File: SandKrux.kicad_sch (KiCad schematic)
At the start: 108 parts, among them CN2 SM02B-PASS-TBT(LF)(SN), CN3 1.25mm-2P socket, IC1 TROPIC01_chip, Q1 S8050, SW1 TL3330AF130QG, SW2 TL3330AF130QG, SW3 TL3330AF130QG, SW4 TL3330AF130QG, SW5 TL3330AF130QG, U10 AXP173_C3345106, U13 CH552T, U2 MT9700, U3 XC6206-3.3V, U9 HX TF-CARD XG8P H1.5

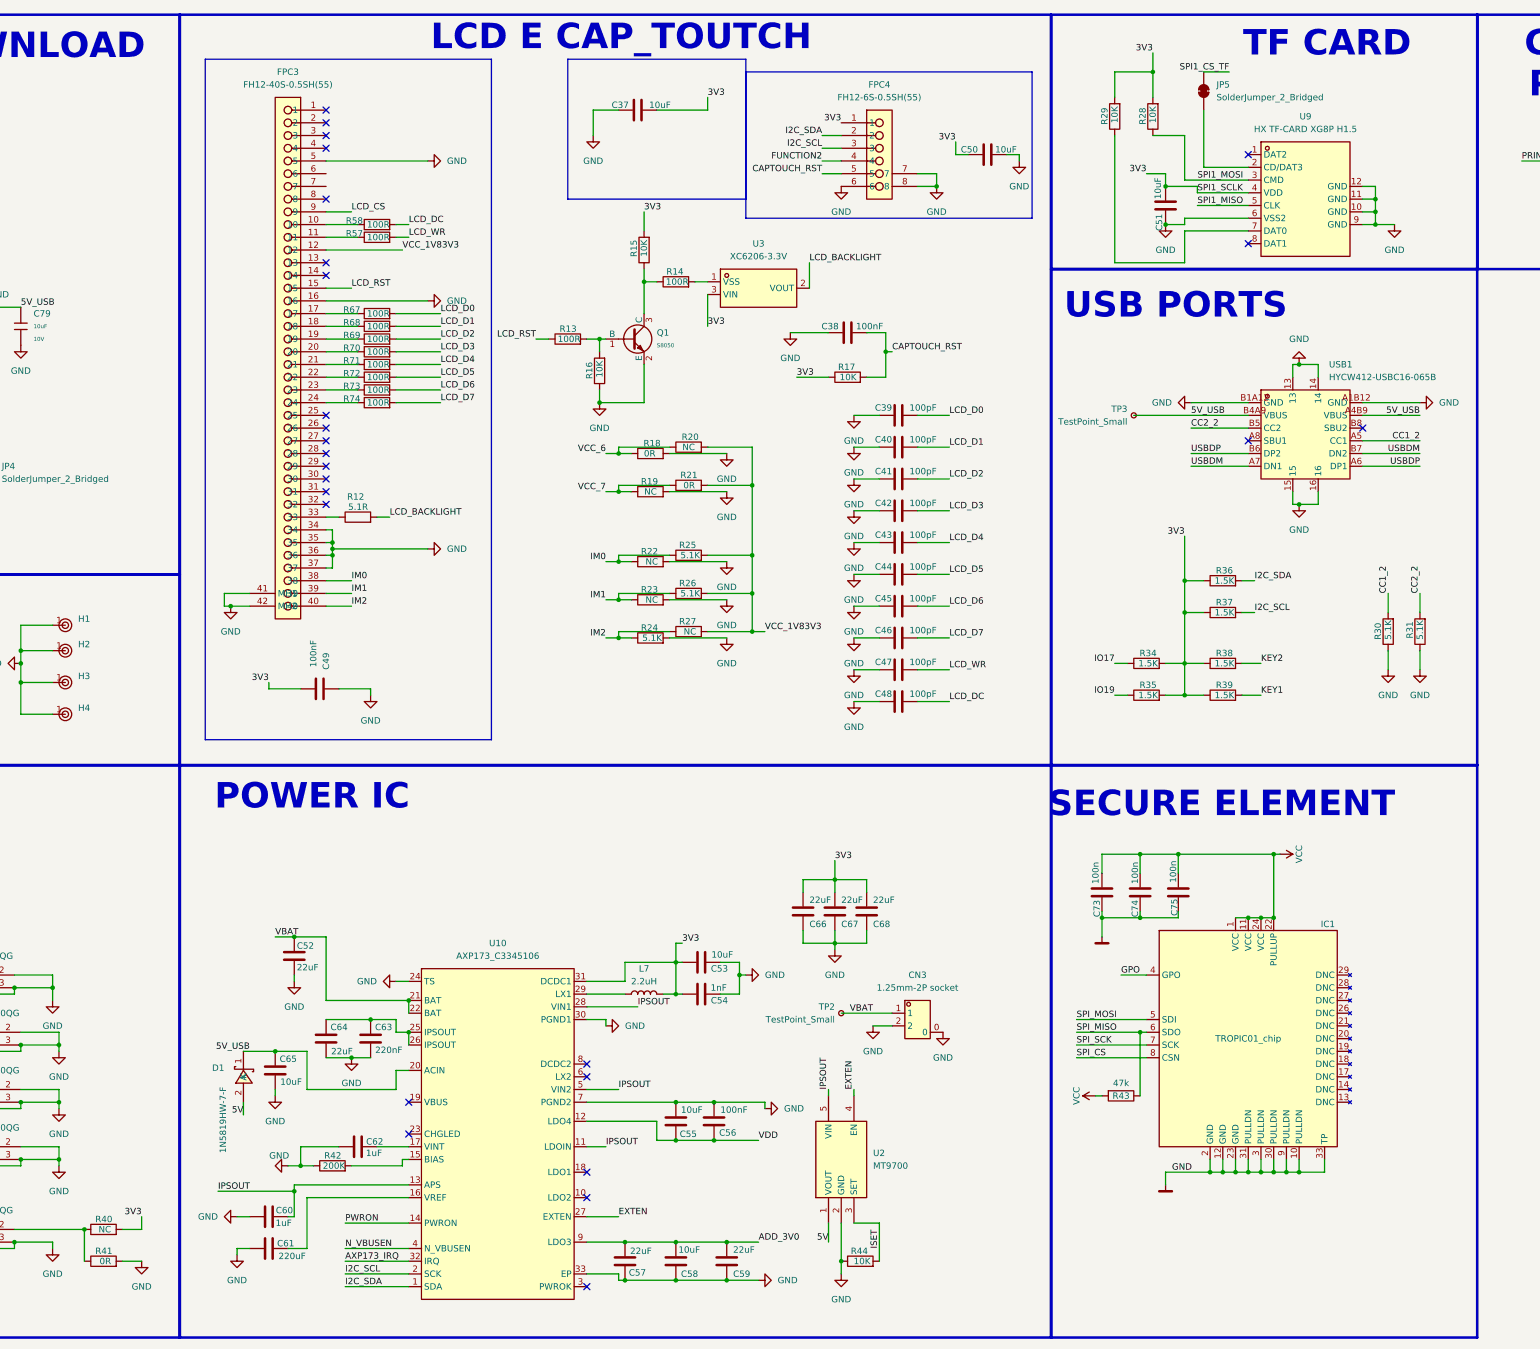
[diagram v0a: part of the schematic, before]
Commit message: troca de resistores por pecas jlcpcb
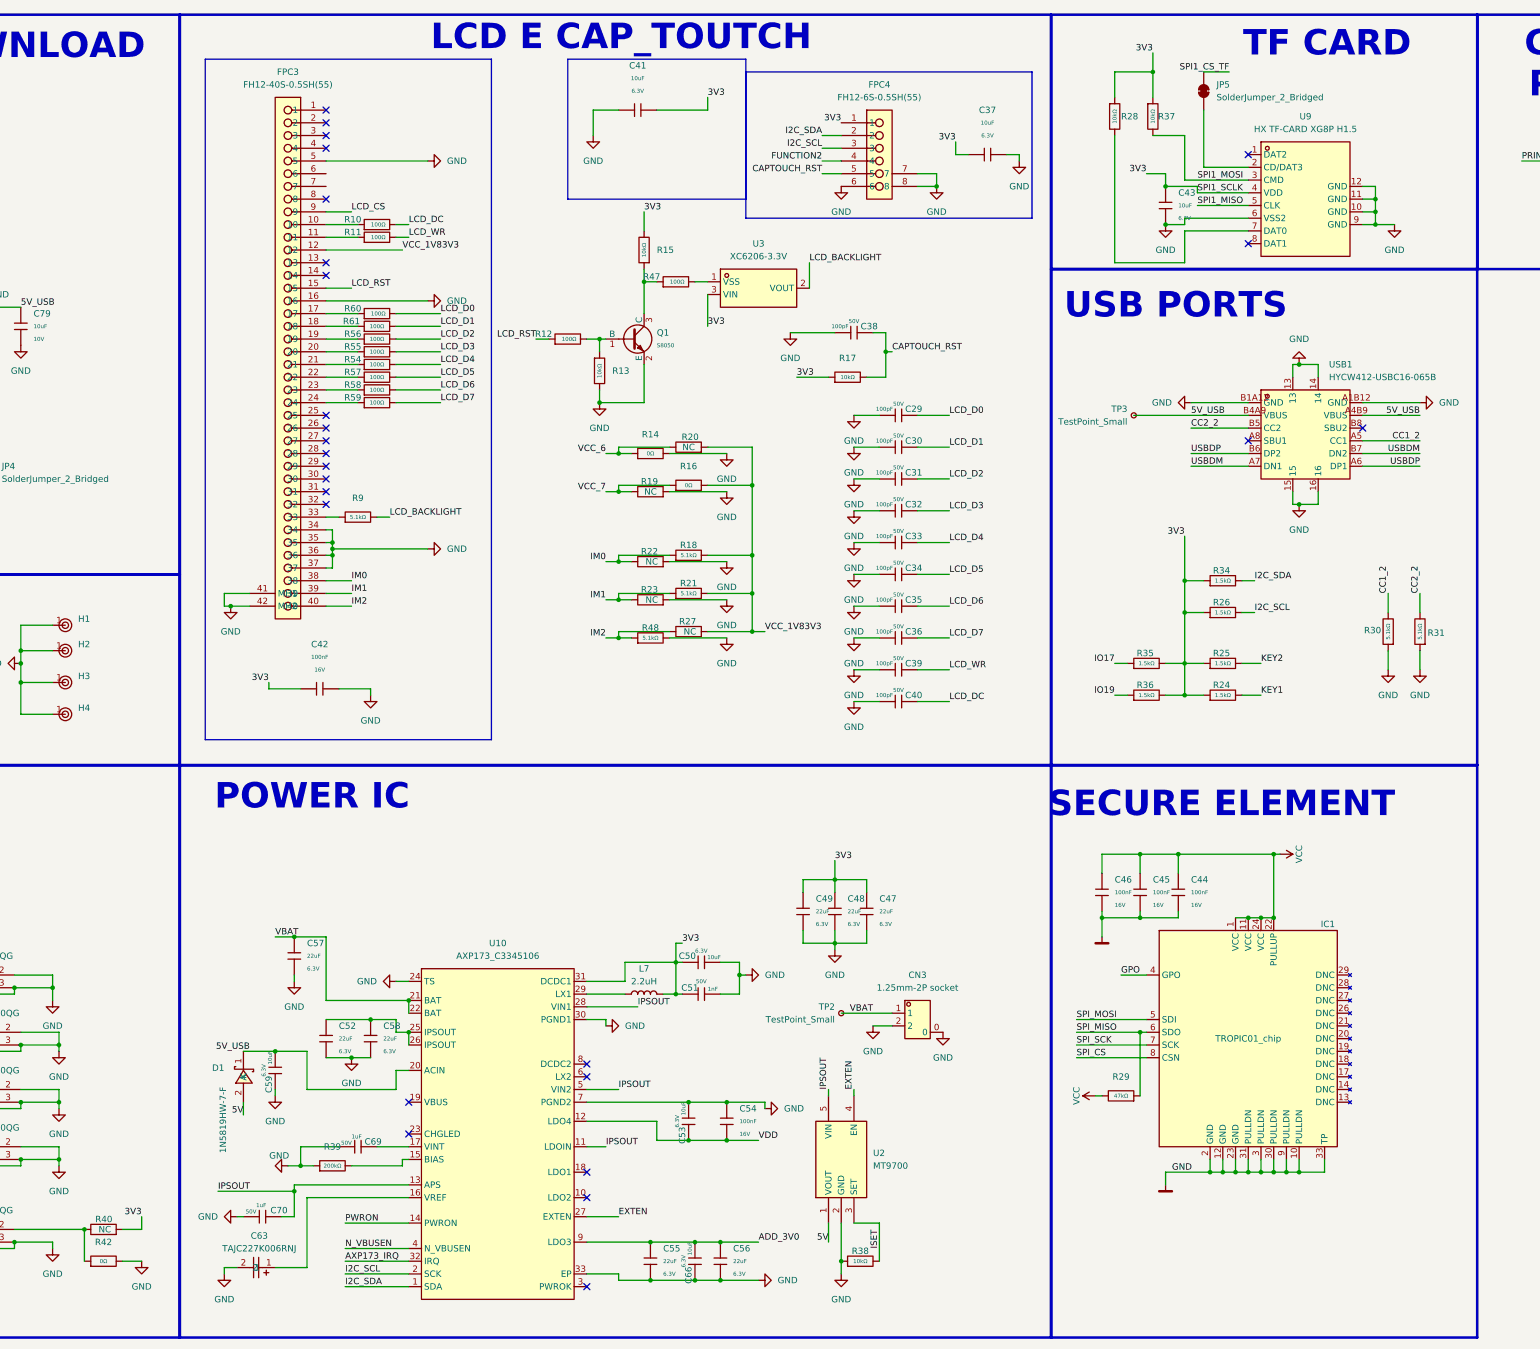
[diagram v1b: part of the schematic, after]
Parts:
- removed C37, C50, C51, C53, C55, C58, C65: 10uF, Capacitor_SMD:C_0201_0603Metric, symbol Device:C
- removed C38, C49, C56: 100nF, Capacitor_SMD:C_0201_0603Metric, symbol Device:C
- removed C39, C40, C41, C42, C43, C44, C45, C46, C47, C48: 100pF, Capacitor_SMD:C_0201_0603Metric, symbol Device:C
- removed C52, C57, C59, C64, C66, C67, C68: 22uF, Capacitor_SMD:C_0201_0603Metric, symbol Device:C
- removed C54: 1nF, Capacitor_SMD:C_0201_0603Metric, symbol Device:C
- removed C60, C62: 1uF, Capacitor_SMD:C_0201_0603Metric, symbol Device:C
- removed C61: 220uF, Capacitor_SMD:C_0201_0603Metric, symbol Device:C
- removed C63: 220nF, Capacitor_SMD:C_0201_0603Metric, symbol Device:C
- removed C73, C74, C75: 100n, Capacitor_SMD:C_0402_1005Metric, symbol Device:C
- removed R12: 5.1R, Resistor_SMD:R_0201_0603Metric, symbol Device:R
- removed R13, R14, R57, R58, R67, R68, R69, R70, R71, R72, R73, R74: 100R, Resistor_SMD:R_0201_0603Metric, symbol Device:R
- removed R15, R16, R17, R28, R29, R44: 10K, Resistor_SMD:R_0201_0603Metric, symbol Device:R
- removed R18, R21, R41: 0R, Resistor_SMD:R_0201_0603Metric, symbol Device:R
- removed R24, R25, R26, R30, R31: 5.1K, Resistor_SMD:R_0201_0603Metric, symbol Device:R
- removed R34, R35, R36, R37, R38, R39: 1.5K, Resistor_SMD:R_0201_0603Metric, symbol Device:R
- removed R42: 200K, Resistor_SMD:R_0201_0603Metric, symbol Device:R
- removed R43: 47k, Resistor_SMD:R_0402_1005Metric, symbol Device:R
- added C29, C30, C31, C32, C33, C34, C35, C36, C38, C39, C40: 100pF, PCM_JLCPCB:C_0402, symbol PCM_JLCPCB-Capacitors:0402,100pF
- added C37, C41, C43, C50, C53, C59, C66: 10uF, PCM_JLCPCB:C_0402, symbol PCM_JLCPCB-Capacitors:0402,10uF
- added C42, C44, C45, C46, C54: 100nF, PCM_JLCPCB:C_0402, symbol PCM_JLCPCB-Capacitors:0402,100nF
- added C47, C48, C49, C52, C55, C56, C57, C58: 22uF, PCM_JLCPCB:C_0603, symbol PCM_JLCPCB-Capacitors:0603,22uF
- added C51: 1nF, PCM_JLCPCB:C_0402, symbol PCM_JLCPCB-Capacitors:0402,1nF
- added C63: TAJC227K006RNJ, easyeda2kicad:CAP-SMD_L6.0-W3.2-R-RD, symbol easyeda2kicad:TAJC227K006RNJ
- added C69, C70: 1uF, PCM_JLCPCB:C_0603, symbol PCM_JLCPCB-Capacitors:0603,1uF
- added R10, R11, R12, R47, R54, R55, R56, R57, R58, R59, R60, R61: 100Ω, PCM_JLCPCB:R_0402, symbol PCM_JLCPCB-Resistors:0402,100Ω
- added R13, R15, R17, R28, R37, R38: 10kΩ, PCM_JLCPCB:R_0402, symbol PCM_JLCPCB-Resistors:0402,10kΩ
- added R14, R16, R42: 0Ω, PCM_JLCPCB:R_0402, symbol PCM_JLCPCB-Resistors:0402,0Ω
- added R18, R21, R30, R31, R48, R9: 5.1kΩ, PCM_JLCPCB:R_0402, symbol PCM_JLCPCB-Resistors:0402,5.1kΩ
- added R24, R25, R26, R34, R35, R36: 1.5kΩ, PCM_JLCPCB:R_0402, symbol PCM_JLCPCB-Resistors:0402,1.5kΩ
- added R29: 47kΩ, PCM_JLCPCB:R_0402, symbol PCM_JLCPCB-Resistors:0402,47kΩ
- added R39: 200kΩ, PCM_JLCPCB:R_0402, symbol PCM_JLCPCB-Resistors:0402,200kΩ
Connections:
- net 3V3: now also C37.1, C41.2, C42.1, C43.1, C47.1, C48.1, C49.1, C50.1, C51.1, R15.2, R17.1, R24.1, R25.1, R26.1, R28.1, R34.1, R35.2, R36.2, R37.1
- net 5V_USB: now also C59.2
- net ADD_3V0: now also C55.1, C56.1, C66.2
- net CAPTOUCH_RST: now also C38.2, R17.2
- net CC1_2: now also R30.2
- net CC2_2: now also R31.2
- net GND: now also C29.1, C30.1, C31.1, C32.1, C33.1, C34.1, C35.1, C36.1, C37.2, C38.1, C39.1, C40.1, C41.1, C42.2, C43.2, C44.2, C45.2, C46.2, C47.2, C48.2, C49.2, C50.2, C51.2, C52.2, C53.2, C54.1, C55.2, C56.2, C57.2, C58.2, C59.1, C63.2, C66.1, C69.1, C70.1, R13.2, R14.2, R30.1, R31.1, R38.1, R39.1, R42.2, R48.2
- net I2C_SCL: now also R26.2
- net I2C_SDA: now also R34.2
- net IM0: now also R18.1
- net IM1: now also R21.1
- net IM2: now also R48.1
- net IO17: now also R35.1
- net IO19: now also R36.1
- net IPSOUT: now also C70.2
- net ISET: now also R38.2
- net KEY1: now also R24.2
- net KEY2: now also R25.2
- net LCD_BACKLIGHT: now also R9.2
- net LCD_D0: now also C29.2, R60.2
- net LCD_D1: now also C30.2, R61.2
- net LCD_D2: now also C31.2, R56.2
- net LCD_D3: now also C32.2, R55.2
- net LCD_D4: now also C33.2, R54.2
- net LCD_D5: now also C34.2, R57.2
- net LCD_D6: now also C35.2, R58.2
- net LCD_D7: now also C36.2, R59.2
- net LCD_DC: now also C40.2, R10.2
- net LCD_RST: now also R12.1
- net LCD_WR: now also C39.2, R11.2
- net SPI1_MOSI: now also R37.2
- net SPI_MISO: now also R29.1
- net VBAT: now also C57.1
- net VCC: now also C44.1, C45.1, C46.1, R29.2
- net VCC_1V83V3: now also R16.2, R18.2, R21.2
- net VCC_6: now also R14.1
- net VCC_7: now also R16.1
- net VDD: now also C53.1, C54.2
- net at Q1.1 (B): now also R12.2, R13.1
- net at U10.15 (BIAS): now also R39.2
- net at U10.16 (VREF): now also C63.1
- net at U10.17 (VINT): now also C69.2
- net at U10.25 (IPSOUT), U10.26 (IPSOUT): now also C52.1, C58.1
- net at FPC3.21: now also R54.1
- net at Q1.3 (C): now also R15.1, R47.1
- net at U3.1 (VSS): now also R47.2
- net at R40.1, SW5.2: now also R42.1
- net at FPC3.10: now also R10.1
- net at FPC3.17: now also R60.1
- net at FPC3.33: now also R9.1
- net at FPC3.19: now also R56.1
- net at U9.7 (DAT0): now also R28.2
- net at FPC3.18: now also R61.1
- net at FPC3.20: now also R55.1
- net at FPC3.24: now also R59.1
- net at FPC3.23: now also R58.1
- net at FPC3.11: now also R11.1
- net at FPC3.22: now also R57.1

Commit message: TROPCAL 01 CONECTIO E ATUALIZACAO E SUBSTITUICAO DE COMPONENTES POR COMPONENTES JLC DISPONIVEIS
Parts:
- removed IC1: TROPIC01_chip, tropic01_chip:QFN-32-1EP_4x4mm_P0.4mm_EP2.65x2.65mm, symbol tropicsquare:TROPIC01_chip_pub
- removed U2: MT9700, easyeda2kicad:SOT-23-5_L3.0-W1.7-P0.95-LS2.8-BR, symbol easyeda2kicad:MT9700
- added IC1: TR01-P2, Package_DFN_QFN:QFN-32-1EP_4x4mm_P0.4mm_EP2.65x2.65mm, symbol TROPIC01:TR01-P2
- added U7: MT9700-N, easyeda2kicad:SOT-23-5_L2.9-W1.6-P0.95-LS2.9-BL, symbol easyeda2kicad:MT9700-N
- SW1, SW2, SW3, SW4, SW5: LCSC Part C2886885 -> C2886886
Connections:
- net VCC is gone; now on net 3V3: C44.1, C45.1, C46.1, R29.2
- net 3V3: now also IC1.1 (VCC), IC1.11 (VCC), IC1.22 (PULLUP), IC1.24 (VCC)
- net 5V: now also U7.1 (VOUT)
- net EXTEN: now also U7.4 (EN)
- net GND: now also IC1.10 (PULLDN), IC1.12 (GND), IC1.2 (GND), IC1.23 (GND), IC1.3 (PULLDN), IC1.30 (PULLDN), IC1.31 (PULLDN), IC1.33 (TP), IC1.9 (PULLDN), U7.2 (GND)
- net IPSOUT: now also U7.5 (VIN)
- net ISET: now also U7.3 (SET)
- net SPI_MISO renamed TP_SPI_MISO
- net TP_SPI_MISO: now also IC1.6 (SDO)
- new net TP_GPO: IC1.4 (GPO)
- new net TP_SPI_CS: IC1.8 (CSN)
- new net TP_SPI_MOSI: IC1.5 (SDI)
- new net TP_SPI_SCK: IC1.7 (SCK)
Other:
- sheet k210 ports: added IO_11, IO_13, IO_15, IO_17, IO_9; removed none
- moved on the sheet: R29
